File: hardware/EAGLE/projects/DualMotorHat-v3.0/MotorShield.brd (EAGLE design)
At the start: 100 x 80 mm, 84 parts, among them IC0 TEENSY_3.1-3.2_ALL_PINS&PADS, IC2_0_PC JP, U0-C1 0.1uF, U0-C2 1nF, U0-C3 0.22uF, U0-C4 0.1uF, U0-C5 0.22uF, U0-R1 4.7k, U0-R2 47k, U0-R3 10k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

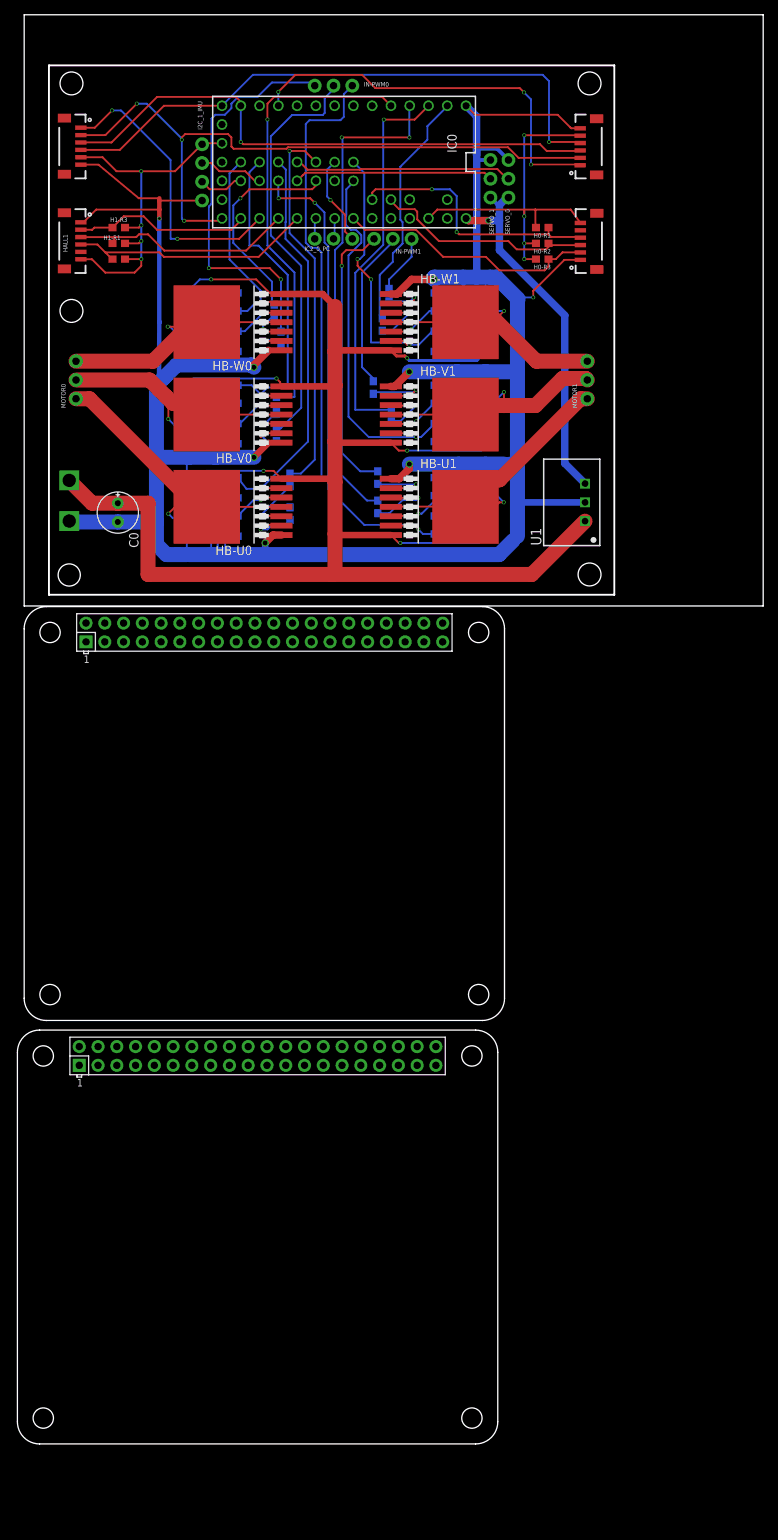
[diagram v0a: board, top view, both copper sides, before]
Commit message: Connector for Hat added
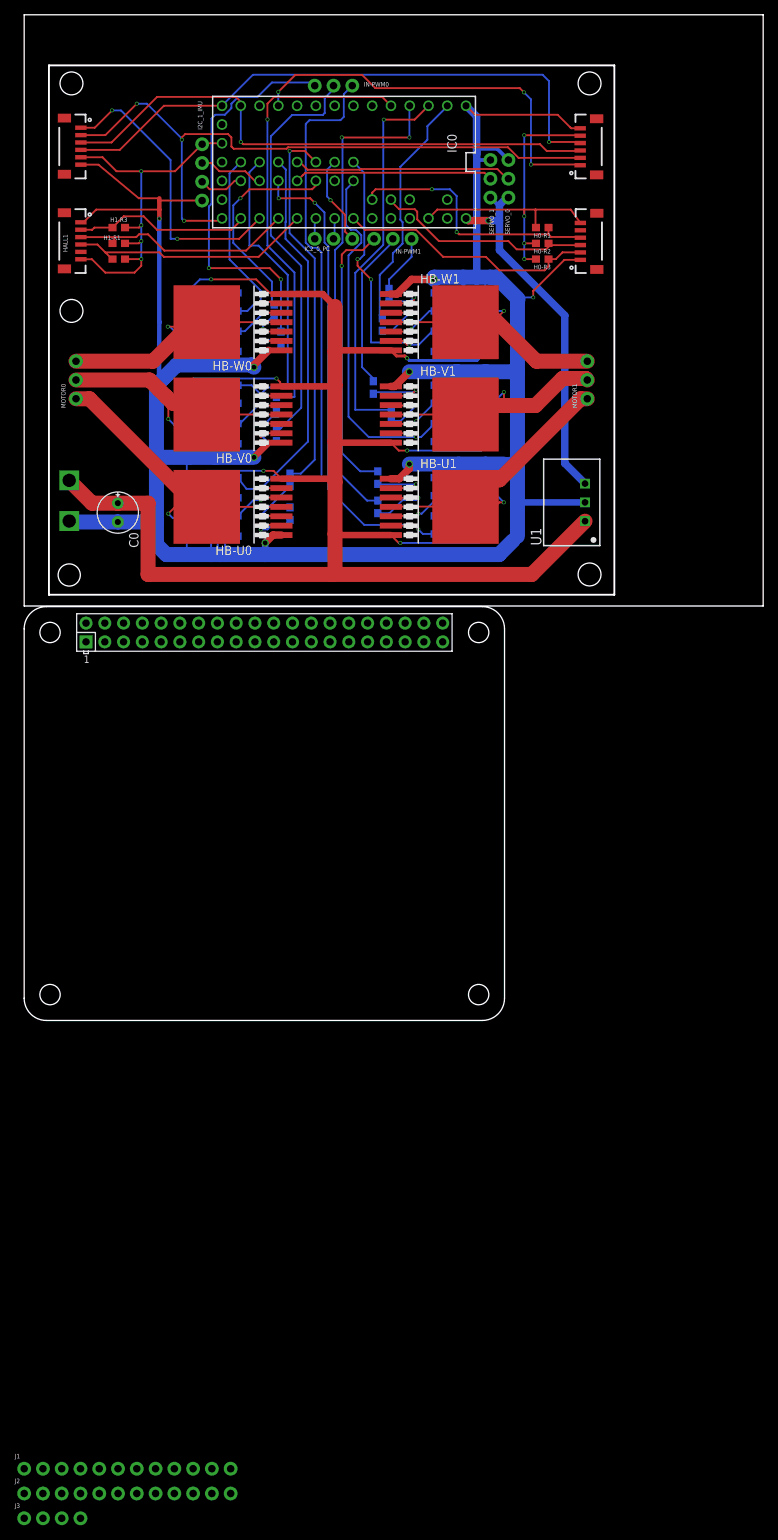
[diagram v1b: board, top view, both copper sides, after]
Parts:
- removed X2: RASPI_BOARD_B+_H, raspberrypi_bastelstube_v13:RASPI_BOARD_B+HAT
- added J1, J2: (no value), SparkFun-Connectors:1X12_NO_SILK
- added J3: (no value), SparkFun-Connectors:1X04_NO_SILK
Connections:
- removed net CS1: IC0.9, SPI_CONN0.1
- removed net CS2: IC0.15/A1, SPI_CONN1.1
- removed net MISO: IC0.12, SPI_CONN0.4, SPI_CONN1.4
- removed net MOSI: IC0.11, SPI_CONN0.3, SPI_CONN1.3
- removed net SCK: IC0.13, SPI_CONN0.2, SPI_CONN1.2
- removed net SCL0: IC0.19/A5, IC2_0_PC.2
- removed net SCL1: I2C_1_IMU.2, IC0.29
- removed net SDA0: IC0.18/A4, IC2_0_PC.1
- removed net SDA1: I2C_1_IMU.3, IC0.30
- new net I2C0_SCL: IC0.19/A5, IC2_0_PC.2, X1.5
- new net I2C0_SDA: IC0.18/A4, IC2_0_PC.1, X1.3
- new net I2C1_SCL: I2C_1_IMU.2, IC0.29, X1.28
- new net I2C1_SDA: I2C_1_IMU.3, IC0.30, X1.27
- new net N$4: J3.4
- new net N$5: J3.3
- new net N$6: J3.2
- new net N$7: J3.1
- new net SPI_CS0: IC0.9, SPI_CONN0.1, X1.24
- new net SPI_CS1: IC0.15/A1, SPI_CONN1.1, X1.26
- new net SPI_MISO: IC0.12, SPI_CONN0.4, SPI_CONN1.4, X1.21
- new net SPI_MOSI: IC0.11, SPI_CONN0.3, SPI_CONN1.3, X1.19
- new net SPI_SCLK: IC0.13, SPI_CONN0.2, SPI_CONN1.2, X1.23
- new net S_PWM_0: SERVO_0.2
- net 3V3: no longer X2.1
- net 5V0: no longer X2.2
- net GND: no longer X2.6
- net HALL_U0: now also J1.1
- net HALL_V0: now also J1.2
- net HALL_W0: now also J1.3
- net INH_U0: now also J1.7
- net INH_V0: now also J1.8
- net INH_W0: now also J1.9
- net IN_U0: now also J1.4
- net IN_V0: now also J1.5
- net IN_W0: now also J1.6
- net IS_U0: now also J1.10
- net IS_V0: now also J1.11
- net IS_W0: now also J1.12
- net S_PWM_2: no longer SERVO_0.2
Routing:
- net SPI_SCLK: track 0.00 -> 90.5 mm, vias 0 -> 3
- net SCK: track 90.5 -> 0.00 mm, vias 3 -> 0
- net SPI_MISO: track 0.00 -> 80.5 mm, vias 0 -> 1
- net MISO: track 80.5 -> 0.00 mm, vias 1 -> 0
- net SPI_MOSI: track 0.00 -> 76.4 mm, vias 0 -> 1
- net MOSI: track 76.4 -> 0.00 mm, vias 1 -> 0
- net SPI_CS0: track 0.00 -> 53.9 mm, vias 0 -> 3
- net CS1: track 53.9 -> 0.00 mm, vias 3 -> 0
- net SPI_CS1: track 0.00 -> 39.7 mm, vias 0 -> 2
- net CS2: track 39.7 -> 0.00 mm, vias 2 -> 0
- net SDA1: track 8.77 -> 0.00 mm
- net I2C1_SDA: track 0.00 -> 8.77 mm
- net SCL1: track 6.13 -> 0.00 mm
- net I2C1_SCL: track 0.00 -> 6.13 mm
- net SDA0: track 2.83 -> 0.00 mm
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
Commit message: layout update
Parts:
- removed IC0: TEENSY_3.1-3.2_ALL_PINS&PADS, Teensy_3_and_LC_Series_Boards_v1.4:TEENSY_3.0-3.2_ALL_PINS_&_PADS
- removed IN-PWM0, IN-PWM1: JP, SparkFun-Connectors:1X03_NO_SILK
- removed J1, J2: (no value), SparkFun-Connectors:1X12_NO_SILK
- removed J3: (no value), SparkFun-Connectors:1X04_NO_SILK
- removed U$5: 5569-002, 5569-02:5569-002
- added BATTERY: (no value), SparkFun-Connectors:1X03_NO_SILK
- added MOTOR_CONTROL_1, MOTOR_CONTRO_0: (no value), SparkFun-Connectors:1X12_NO_SILK
- added SERVOS, VCC: (no value), SparkFun-Connectors:1X02_NO_SILK
- moved HALL0 81.7 mm to (3.17, 13.3), turned to 270 degrees
- moved SERVO_1 78.4 mm to (10.2, 2.54), turned to 0 degrees
- moved SERVO_0 77.8 mm to (10.2, 5.71), turned to 0 degrees
- moved SPI_CONN0 76.1 mm to (3.17, 41.9), turned to 270 degrees
- moved H1-R3 73.2 mm to (81.3, 25.4)
- moved H1-R2 71.3 mm to (81.3, 29.2)
- moved H1-R1 69.9 mm to (81.3, 33.0)
- moved U1-R1 67.8 mm to (53.3, 77.5), flipped to the top
- moved U0-R1 66.9 mm to (5.08, 77.5), flipped to the top, turned to 0 degrees
- moved U0-C2 66.7 mm to (10.2, 73.7), flipped to the top, turned to 0 degrees
- moved HALL1 65.9 mm to (61.6, 13.3), turned to 90 degrees
- moved U0-R2 65.6 mm to (5.08, 73.7), flipped to the top, turned to 0 degrees
- moved U1-C1 65.3 mm to (58.4, 77.5), flipped to the top, turned to 0 degrees
- moved U0-C1 62.7 mm to (10.2, 77.5), flipped to the top
- moved U0-R4 61.8 mm to (5.08, 66.0), flipped to the top, turned to 0 degrees
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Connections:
- removed net AGND: IC0.AGND
- removed net AREF: IC0.AREF
- removed net HALL_U2: H1-R3.1, HALL1.2, IC0.14/A0
- removed net HALL_V2: H1-R2.1, HALL1.3, IC0.16/A2
- removed net HALL_W2: H1-R1.1, HALL1.4, IC0.17/A3
- removed net IN_U2_EX: IC0.21/A7
- removed net IN_U_EX: IC0.5
- removed net IN_V2_EX: IC0.22/A8
- removed net IN_V_EX: IC0.6
- removed net IN_W2_EX: IC0.23/A9
- removed net IN_W_EX: IC0.10
- removed net N$4: J3.4
- removed net N$5: J3.3
- removed net N$6: J3.2
- removed net N$7: J3.1
- removed net S_PWM_0: SERVO_0.2
- removed net S_PWM_1: IC0.32, SERVO_1.2
- removed net S_PWM_2: IC0.25
- removed net VBAT: IC0.VBAT
- removed net VUSB: IC0.VUSB
- new net HALL_U1: H1-R3.1, HALL1.2, MOTOR_CONTROL_1.1
- new net HALL_V1: H1-R2.1, HALL1.3, MOTOR_CONTROL_1.2
- new net HALL_W1: H1-R1.1, HALL1.4, MOTOR_CONTROL_1.3
- new net SERVO_0: SERVOS.1, SERVO_0.2
- new net SERVO_1: SERVOS.2, SERVO_1.2
- net 3.3V: no longer IC0.3.3V, IC0.3.3V1, IC0.3.3V2
- net GND: now also BATTERY.1, VCC.1; no longer IC0.GND, IC0.GND1, IC0.GND2, U$5.GND
- net HALL_U0: now also MOTOR_CONTRO_0.1; no longer IC0.20/A6, J1.1
- net HALL_V0: now also MOTOR_CONTRO_0.2; no longer IC0.A10, J1.2
- net HALL_W0: now also MOTOR_CONTRO_0.3; no longer IC0.A11, J1.3
- net I2C0_SCL: no longer IC0.19/A5
- net I2C0_SDA: no longer IC0.18/A4
- net I2C1_SCL: no longer IC0.29
- net I2C1_SDA: no longer IC0.30
- net INH_U0: now also MOTOR_CONTRO_0.7; no longer IC0.24, J1.7
- net INH_U1: now also MOTOR_CONTROL_1.7; no longer IC0.2
- net INH_V0: now also MOTOR_CONTRO_0.8; no longer IC0.3, J1.8
- net INH_V1: now also MOTOR_CONTROL_1.8; no longer IC0.1
- net INH_W0: now also MOTOR_CONTRO_0.9; no longer IC0.33, J1.9
- net INH_W1: now also MOTOR_CONTROL_1.9; no longer IC0.0
- net IN_U0: now also MOTOR_CONTRO_0.4; no longer IN-PWM0.3, J1.4
- net IN_U1: now also MOTOR_CONTROL_1.4; no longer IN-PWM1.3
- net IN_V0: now also MOTOR_CONTRO_0.5; no longer IN-PWM0.2, J1.5
- net IN_V1: now also MOTOR_CONTROL_1.5; no longer IN-PWM1.2
- net IN_W0: now also MOTOR_CONTRO_0.6; no longer IN-PWM0.1, J1.6
- net IN_W1: now also MOTOR_CONTROL_1.6; no longer IN-PWM1.1
- net IS_U0: now also MOTOR_CONTRO_0.10; no longer IC0.26, J1.10
- net IS_U1: now also MOTOR_CONTROL_1.10; no longer IC0.31
- net IS_V0: now also MOTOR_CONTRO_0.11; no longer IC0.27, J1.11
- net IS_V1: now also MOTOR_CONTROL_1.11; no longer IC0.A13
- net IS_W0: now also MOTOR_CONTRO_0.12; no longer IC0.28, J1.12
- net IS_W1: now also MOTOR_CONTROL_1.12; no longer IC0.A12
- net SPI_CS0: no longer IC0.9
- net SPI_CS1: no longer IC0.15/A1
- net SPI_MISO: no longer IC0.12
- net SPI_MOSI: no longer IC0.11
- net SPI_SCLK: no longer IC0.13
- net VCC: now also VCC.2; no longer IC0.VIN
- net VI: now also BATTERY.3; no longer U$5.VCC
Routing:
- net GND: track 465.2 -> 152.4 mm, vias 9 -> 3
- net 3.3V: track 103.3 -> 0.00 mm, vias 8 -> 0
- net VI: track 271.9 -> 176.7 mm
- net SPI_SCLK: track 90.5 -> 0.00 mm, vias 3 -> 0
- net SPI_MISO: track 80.5 -> 0.00 mm, vias 1 -> 0
- net SPI_MOSI: track 76.4 -> 0.00 mm, vias 1 -> 0
- net IS_U1: track 70.3 -> 0.00 mm, vias 3 -> 0
- net INH_U1: track 66.3 -> 0.00 mm, vias 2 -> 0
- net INH_V0: track 61.2 -> 0.00 mm, vias 1 -> 0
- net IN_U0: track 59.2 -> 0.00 mm
- net IS_U0: track 58.0 -> 0.00 mm, vias 1 -> 0
- net IN_V0: track 55.7 -> 0.00 mm
- net IN_W0: track 54.4 -> 0.00 mm, vias 2 -> 0
- net IS_V1: track 54.2 -> 0.00 mm, vias 1 -> 0
- net SPI_CS0: track 53.9 -> 0.00 mm, vias 3 -> 0
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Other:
- outline, holes or cut-outs redrawn

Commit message: progress on MotorHat
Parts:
- removed MOTOR_CONTROL_1, MOTOR_CONTRO_0: (no value), SparkFun-Connectors:1X12_NO_SILK
- added MOTOR0_CONTROL, MOTOR0_SENS, MOTOR1_CONTROL, MOTOR1_SENS: (no value), SparkFun-Connectors:1X06_NO_SILK
- moved H0-R1 85.5 mm to (3.81, 9.53), flipped to the bottom, turned to 180 degrees
- moved H0-R2 82.3 mm to (3.81, 13.3), flipped to the bottom, turned to 180 degrees
- moved H0-R3 79.7 mm to (3.81, 17.1), flipped to the bottom, turned to 180 degrees
- moved U1-R3 55.9 mm to (52.4, 14.0), flipped to the bottom, turned to 180 degrees
- moved U1-R4 54.6 mm to (52.4, 11.4), flipped to the bottom, turned to 180 degrees
- moved U0-R3 53.8 mm to (12.4, 16.5), flipped to the bottom
- moved U0-R4 47.6 mm to (12.4, 19.1), flipped to the bottom
- moved V1-R3 44.0 mm to (52.7, 27.9), flipped to the bottom, turned to 180 degrees
- moved V1-R4 42.8 mm to (52.7, 25.4), flipped to the bottom, turned to 180 degrees
- moved V0-R3 40.4 mm to (12.4, 30.5), flipped to the bottom
- moved W1-R3 38.8 mm to (53.0, 41.9), flipped to the bottom, turned to 180 degrees
- moved W1-R4 37.9 mm to (53.0, 39.4), flipped to the bottom, turned to 180 degrees
- moved V0-R4 34.3 mm to (12.4, 33.0), flipped to the bottom
- moved W0-R3 33.5 mm to (12.4, 44.5), flipped to the bottom
- moved W0-R4 29.0 mm to (12.4, 47.0), flipped to the bottom
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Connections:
- removed net 3V3: X1.1
- net 3.3V: now also X1.1
- net HALL_U0: now also H0-R1.1, HALL0.4, MOTOR0_SENS.1; no longer H0-R3.1, HALL0.2, MOTOR_CONTRO_0.1
- net HALL_U1: now also H1-R1.1, HALL1.4, MOTOR1_SENS.1; no longer H1-R3.1, HALL1.2, MOTOR_CONTROL_1.1
- net HALL_V0: now also MOTOR0_SENS.2; no longer MOTOR_CONTRO_0.2
- net HALL_V1: now also MOTOR1_SENS.2; no longer MOTOR_CONTROL_1.2
- net HALL_W0: now also H0-R3.1, HALL0.2, MOTOR0_SENS.3; no longer H0-R1.1, HALL0.4, MOTOR_CONTRO_0.3
- net HALL_W1: now also H1-R3.1, HALL1.2, MOTOR1_SENS.3; no longer H1-R1.1, HALL1.4, MOTOR_CONTROL_1.3
- net INH_U0: now also MOTOR0_CONTROL.1; no longer MOTOR_CONTRO_0.7
- net INH_U1: now also MOTOR1_CONTROL.1; no longer MOTOR_CONTROL_1.7
- net INH_V0: now also MOTOR0_CONTROL.2; no longer MOTOR_CONTRO_0.8
- net INH_V1: now also MOTOR1_CONTROL.2; no longer MOTOR_CONTROL_1.8
- net INH_W0: now also MOTOR0_CONTROL.3; no longer MOTOR_CONTRO_0.9
- net INH_W1: now also MOTOR1_CONTROL.3; no longer MOTOR_CONTROL_1.9
- net IN_U0: now also MOTOR0_CONTROL.4; no longer MOTOR_CONTRO_0.4
- net IN_U1: now also MOTOR1_CONTROL.4; no longer MOTOR_CONTROL_1.4
- net IN_V0: now also MOTOR0_CONTROL.5; no longer MOTOR_CONTRO_0.5
- net IN_V1: now also MOTOR1_CONTROL.5; no longer MOTOR_CONTROL_1.5
- net IN_W0: now also MOTOR0_CONTROL.6; no longer MOTOR_CONTRO_0.6
- net IN_W1: now also MOTOR1_CONTROL.6; no longer MOTOR_CONTROL_1.6
- net IS_U0: now also MOTOR0_SENS.4; no longer MOTOR_CONTRO_0.10
- net IS_U1: now also MOTOR1_SENS.4; no longer MOTOR_CONTROL_1.10
- net IS_V0: now also MOTOR0_SENS.5; no longer MOTOR_CONTRO_0.11
- net IS_V1: now also MOTOR1_SENS.5; no longer MOTOR_CONTROL_1.11
- net IS_W0: now also MOTOR0_SENS.6; no longer MOTOR_CONTRO_0.12
- net IS_W1: now also MOTOR1_SENS.6; no longer MOTOR_CONTROL_1.12
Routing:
- net 3.3V: track 0.00 -> 180.3 mm, vias 0 -> 4
- net I2C1_SDA: track 0.00 -> 120.3 mm, vias 0 -> 3
- net GND: track 152.4 -> 266.7 mm, vias 3 -> 7
- net I2C1_SCL: track 0.00 -> 87.6 mm, vias 0 -> 1
- net SPI_SCLK: track 0.00 -> 71.5 mm, vias 0 -> 2
- net SPI_MOSI: track 0.00 -> 71.0 mm, vias 0 -> 4
- net SPI_MISO: track 0.00 -> 70.2 mm, vias 0 -> 2
- net I2C0_SCL: track 0.00 -> 55.6 mm
- net I2C0_SDA: track 0.00 -> 51.5 mm
- net SPI_CS0: track 0.00 -> 39.3 mm
- net VCC: track 0.00 -> 37.2 mm
- net W0: track 0.00 -> 34.0 mm
- net SPI_CS1: track 0.00 -> 33.7 mm
- net U0: track 0.00 -> 31.3 mm
- net U1: track 0.00 -> 30.7 mm
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
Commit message: update
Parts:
- removed VCC: (no value), SparkFun-Connectors:1X02_NO_SILK
- added J1: (no value), SparkFun-Connectors:1X03_NO_SILK
- moved I2C_1_IMU 64.7 mm to (54.6, 48.3), turned to 180 degrees
- moved U0-R1 62.7 mm to (24.1, 17.8), flipped to the bottom
- moved U0-R2 61.4 mm to (24.1, 15.2), flipped to the bottom
- moved U1-R3 57.3 mm to (55.9, 71.1), turned to 0 degrees
- moved U1-R4 57.3 mm to (55.9, 68.6), turned to 0 degrees
- moved V0-R3 45.6 mm to (33.0, 71.1)
- moved V1-R3 44.5 mm to (63.5, 71.1), turned to 0 degrees
- moved V1-R4 44.5 mm to (63.5, 68.6), turned to 0 degrees
- moved IC2_0_PC 43.3 mm to (11.4, 48.3)
- moved V0-R4 41.1 mm to (33.0, 68.6)
- moved W0-R3 38.9 mm to (40.6, 71.1)
- moved W0-R4 35.6 mm to (40.6, 68.6)
- moved W1-R3 34.4 mm to (71.1, 71.1), turned to 0 degrees
- moved W1-R4 34.4 mm to (71.1, 68.6), turned to 0 degrees
- moved U1 29.9 mm to (21.6, 6.99)
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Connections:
- removed net VCC: SERVO_0.3, SERVO_1.3, U1.3, VCC.2
- new net 3V3: X1.1
- new net 5.0V: J1.2, SERVO_0.3, SERVO_1.3, U1.3
- net 3.3V: now also J1.3; no longer X1.1
- net GND: now also J1.1; no longer VCC.1
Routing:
- net 3.3V: track 180.3 -> 0.00 mm, vias 4 -> 0
- net GND: track 266.7 -> 141.2 mm, vias 7 -> 6
- net I2C1_SDA: track 120.3 -> 0.00 mm, vias 3 -> 0
- net I2C1_SCL: track 87.6 -> 0.00 mm, vias 1 -> 0
- net SPI_SCLK: track 71.5 -> 0.00 mm, vias 2 -> 0
- net SPI_MOSI: track 71.0 -> 0.00 mm, vias 4 -> 0
- net SPI_MISO: track 70.2 -> 0.00 mm, vias 2 -> 0
- net I2C0_SCL: track 55.6 -> 0.00 mm
- net VI: track 195.9 -> 140.6 mm, vias 7 -> 0
- net I2C0_SDA: track 51.5 -> 0.00 mm
- net SPI_CS0: track 39.3 -> 0.00 mm
- net VCC: track 37.2 -> 0.00 mm
- net W0: track 34.0 -> 0.00 mm
- net SPI_CS1: track 33.7 -> 0.00 mm
- net U0: track 31.3 -> 0.00 mm
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
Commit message: progress on MotorHat
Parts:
- moved U0-C2 57.3 mm to (26.0, 16.5)
- moved U0-C1 54.8 mm to (26.0, 21.6), turned to 180 degrees
- moved U0-C3 52.8 mm to (30.5, 19.1), turned to 180 degrees
- moved U0-C5 52.8 mm to (30.5, 14.0)
- moved U0-C4 52.8 mm to (30.5, 16.5)
- moved U0-R3 9.67 mm to (21.6, 19.1)
- moved U0-R4 9.67 mm to (21.6, 21.6)
- moved U0-R1 2.29 mm to (26.0, 19.1)
- moved U0-R2 2.29 mm to (26.0, 14.0)
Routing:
- net U0: track 0.00 -> 33.4 mm, vias 0 -> 1
- net VI: track 140.6 -> 156.7 mm, vias 0 -> 1
- net GND: track 141.2 -> 156.7 mm
- net IS_U0: track 0.00 -> 13.0 mm, vias 0 -> 1
- net N$10: track 0.00 -> 11.9 mm, vias 0 -> 1
- net N$11: track 0.00 -> 6.77 mm, vias 0 -> 1
- net N$14: track 0.00 -> 5.56 mm, vias 0 -> 1

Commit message: update
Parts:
- moved U1-R1 63.6 mm to (40.0, 14.6), turned to 180 degrees
- moved U1-C2 61.9 mm to (35.6, 14.0), turned to 180 degrees
- moved U1-R2 59.3 mm to (40.0, 16.5), turned to 180 degrees
- moved U1-C1 58.4 mm to (40.0, 19.1), turned to 180 degrees
- moved U1-C3 57.1 mm to (35.6, 16.5), turned to 180 degrees
- moved U1-R3 55.8 mm to (44.5, 16.5), turned to 180 degrees
- moved U1-R4 55.2 mm to (44.5, 14.6), turned to 180 degrees
- moved U1-C4 52.2 mm to (35.6, 19.1), turned to 180 degrees
- moved V1-C2 49.8 mm to (40.0, 27.9)
- moved V1-C1 49.5 mm to (35.6, 33.0)
- moved V1-R1 49.2 mm to (40.0, 33.0)
- moved V1-R2 49.2 mm to (40.0, 30.5)
- moved U1-C5 47.4 mm to (35.6, 21.6), turned to 180 degrees
- moved V1-C5 47.3 mm to (35.6, 25.4)
- moved V1-C3 47.3 mm to (35.6, 30.5)
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- renumbered J1 to VCC
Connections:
- net N$1 renamed HB_INH_W0
- net N$10 renamed SR_U0
- net N$11 renamed HB_INH_U0
- net N$14 renamed HB_IN_U0
- net N$17 renamed HB_INH_U1
- net N$18 renamed HB_INH_V0
- net N$19 renamed HB_IN_U1
- net N$2 renamed SR_V0
- net N$20 renamed HB_IN_W0
- net N$23 renamed SR_U1
- net N$24 renamed HB_IN_V0
- net N$26 renamed HB_INH_V1
- net N$27 renamed HB_IN_V1
- net N$29 renamed SR_V1
- net N$3 renamed SR_W0
- net N$30 renamed HB_INH_W1
- net N$31 renamed HB_IN_W1
- net N$33 renamed SR_W1
- net GND: now also U0-C1.1, U0-C4.1, U1-C1.1, U1-C4.1, V0-C1.1, V0-C4.1, V1-C1.1, V1-C4.1, W0-C1.1, W0-C4.1, W1-C1.1, W1-C4.1; no longer U0-C1.2, U0-C4.2, U1-C1.2, U1-C4.2, V0-C1.2, V0-C4.2, V1-C1.2, V1-C4.2, W0-C1.2, W0-C4.2, W1-C1.2, W1-C4.2
- net IS_U0: now also U0-C1.2; no longer U0-C1.1
- net IS_U1: now also U1-C1.2; no longer U1-C1.1
- net IS_V0: now also V0-C1.2; no longer V0-C1.1
- net IS_V1: now also V1-C1.2; no longer V1-C1.1
- net IS_W0: now also W0-C1.2; no longer W0-C1.1
- net IS_W1: now also W1-C1.2; no longer W1-C1.1
- net VI: now also U0-C4.2, U1-C4.2, V0-C4.2, V1-C4.2, W0-C4.2, W1-C4.2; no longer U0-C4.1, U1-C4.1, V0-C4.1, V1-C4.1, W0-C4.1, W1-C4.1
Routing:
- net VI: track 156.7 -> 222.3 mm, vias 1 -> 3
- net GND: track 156.7 -> 222.0 mm
- net 5.0V: track 0.00 -> 40.6 mm, vias 0 -> 1
- net V0: track 0.00 -> 30.7 mm, vias 0 -> 1
- net W0: track 0.00 -> 20.6 mm, vias 0 -> 1
- net IS_V0: track 0.00 -> 19.2 mm, vias 0 -> 1
- net IS_W0: track 0.00 -> 19.1 mm, vias 0 -> 1
- net SR_V0: track 0.00 -> 11.8 mm, vias 0 -> 1
- net SR_W0: track 0.00 -> 11.8 mm, vias 0 -> 1
- net HB_INH_W0: track 0.00 -> 6.65 mm, vias 0 -> 1
- net HB_INH_V0: track 0.00 -> 6.65 mm, vias 0 -> 1
- net IS_U0: track 13.0 -> 19.2 mm
- net HB_IN_W0: track 0.00 -> 5.50 mm, vias 0 -> 1
- net HB_IN_V0: track 0.00 -> 5.50 mm, vias 0 -> 1
- net U0: track 33.4 -> 32.5 mm
